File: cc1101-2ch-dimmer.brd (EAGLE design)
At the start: 57.7 x 56.6 mm, 26 parts, among them Q1 IRLZ44, Q2 IRLZ44, U1 ATMEGA328P-AU, U2 0ZCG0035AF2C, U3 173950378, X2 MSTBA2, X3 MSTBA2, X4 MSTBA2

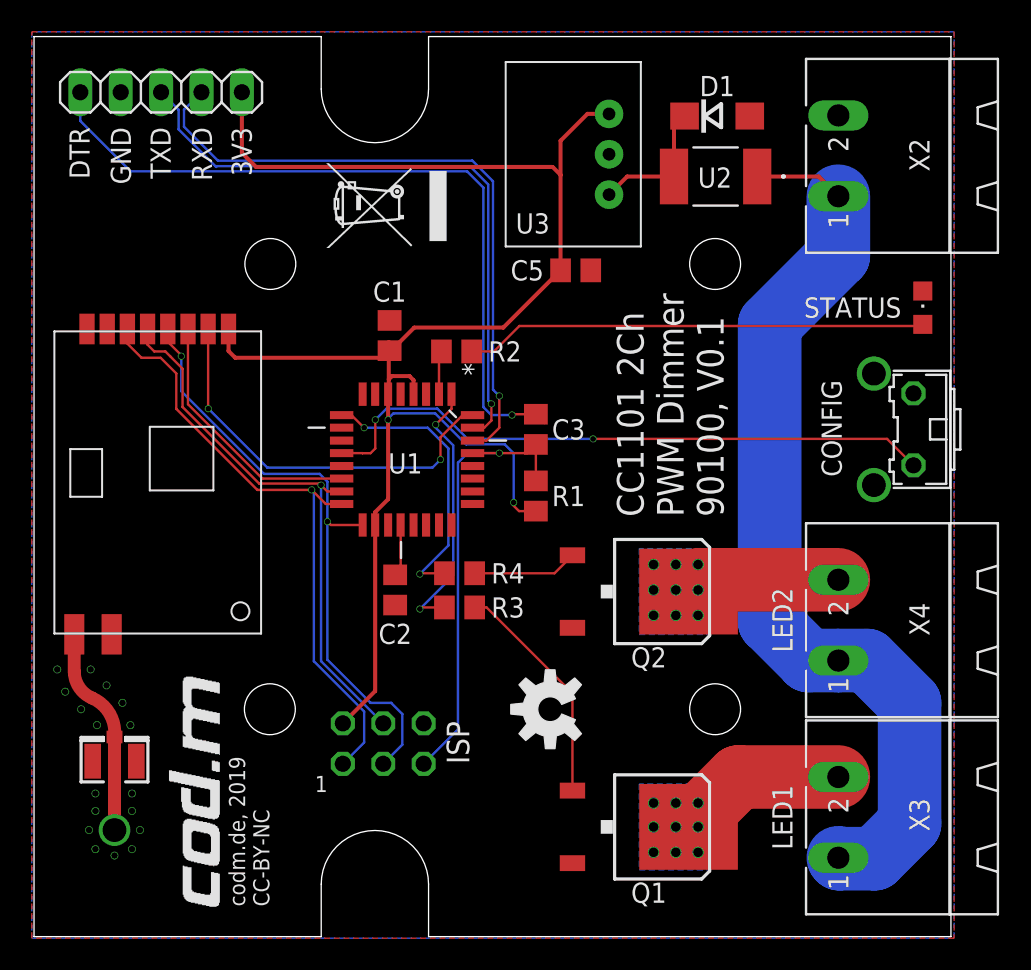
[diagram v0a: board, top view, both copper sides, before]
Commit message: reworked texts
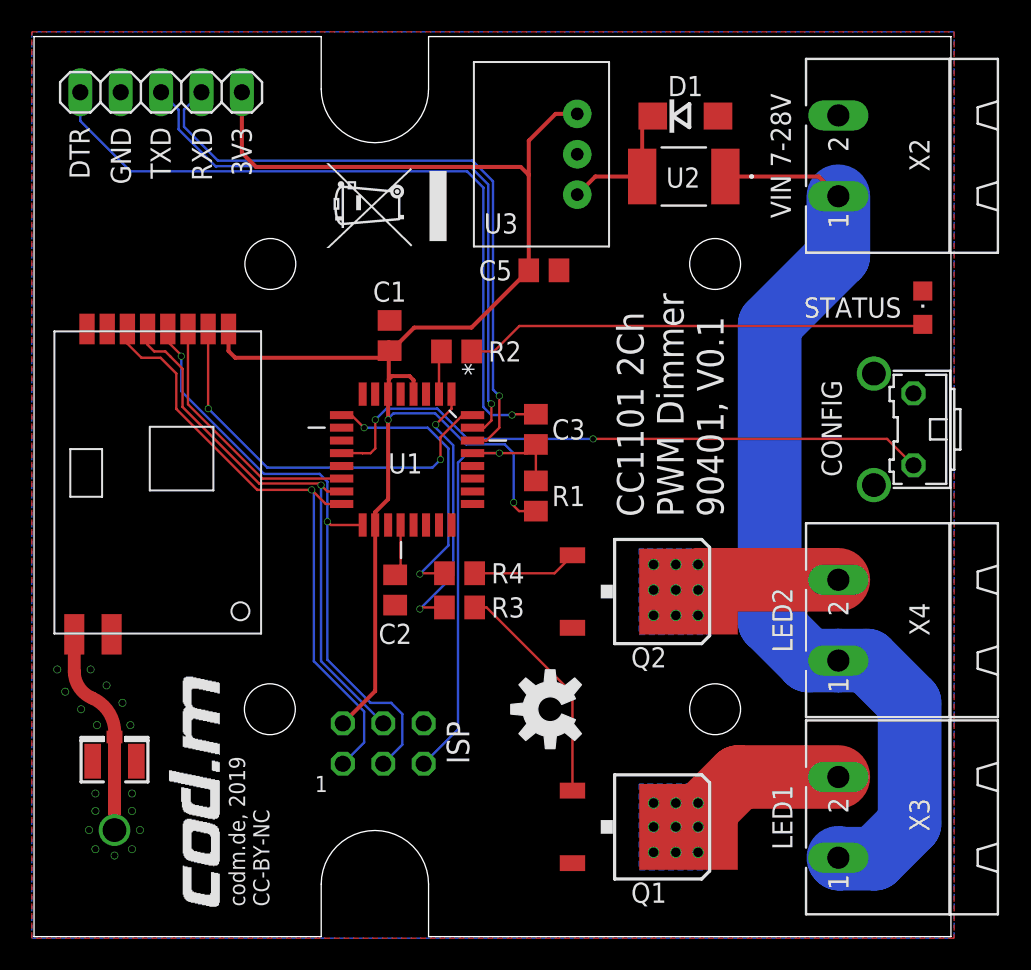
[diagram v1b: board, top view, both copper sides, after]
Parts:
- moved C5 2.00 mm to (32.2, 42.0)
- moved D1 2.00 mm to (41.1, 51.7)
- moved U2 2.00 mm to (41.0, 47.9)
- moved U3 2.00 mm to (36.3, 49.3)
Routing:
- net +3V: track 102.9 -> 98.9 mm
- net VCC: track 58.2 -> 60.2 mm
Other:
- board text added: "CC1101 2Ch PWM Dimmer 90401, V0.1"
- board text added: "VIN 7-28V"
- board text removed: "7-28V"
- board text removed: "CC1101 2Ch PWM Dimmer 90100, V0.1"

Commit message: added 8mhz resonator, reworked for 0.2
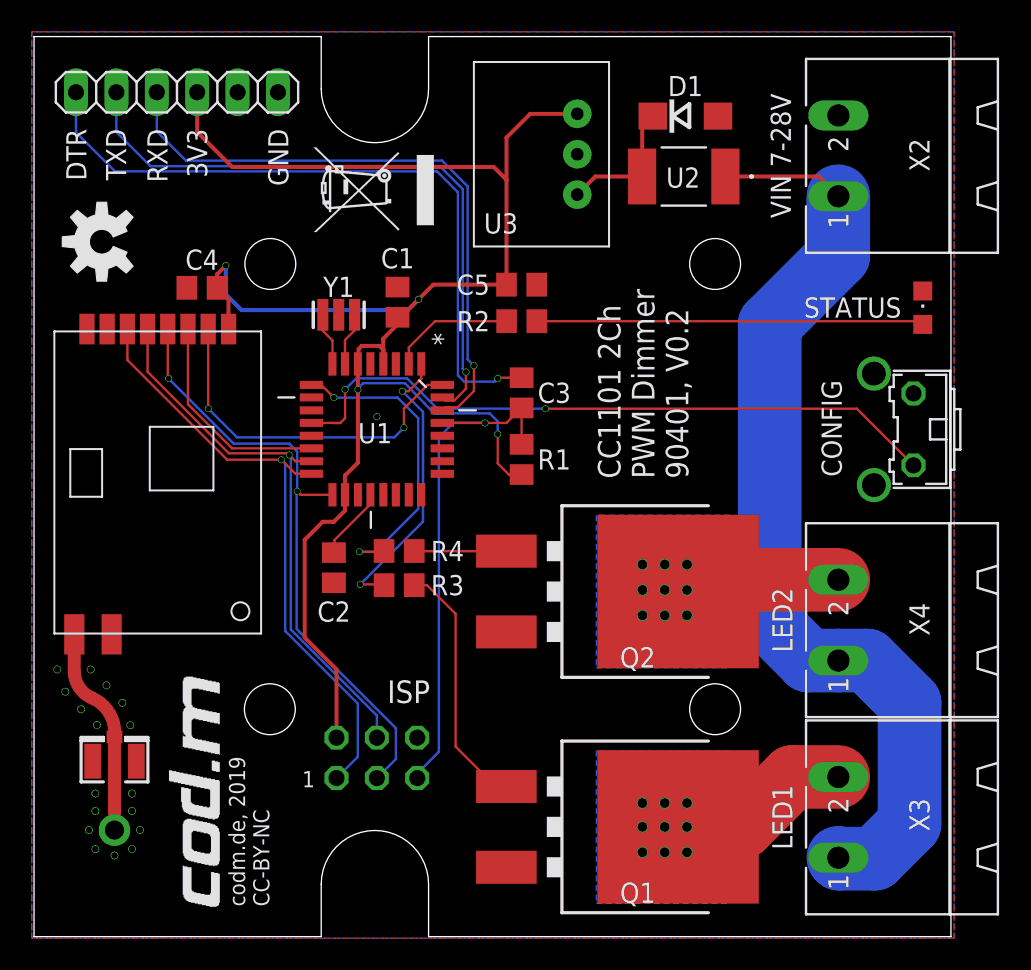
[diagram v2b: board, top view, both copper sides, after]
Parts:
- added C4: 100n, rcl:C0805
- added Y1: CSTCE8M00G52, SmartPrj:RESONATOR
- JP3: device pinhead:1X05 -> pinhead:1X06
- Q1, Q2: value IRLZ44 -> IRLZ44NS; device codm:D-PAK_TO252AA -> codm:D2PAK
- moved LOGO1 40.7 mm to (4.40, 43.8)
- moved R2 4.52 mm to (30.8, 38.8)
- moved C2 4.10 mm to (19.0, 23.3)
- moved R4 4.05 mm to (23.1, 24.4)
- moved R3 4.05 mm to (23.1, 22.2)
- moved U1 2.69 mm to (21.7, 32.0)
- moved R1 2.47 mm to (30.8, 30.1)
- moved C3 2.47 mm to (30.8, 34.3)
- moved C1 2.16 mm to (23.0, 40.0)
- moved C5 1.66 mm to (30.8, 41.1)
- moved U$3 1.28 mm to (25.3, 44.4)
- moved JP3 1.00 mm to (9.13, 53.2)
- moved JP1 0.98 mm to (21.7, 11.3)
- moved Q1 0.70 mm to (38.1, 7.00)
- moved Q2 0.70 mm to (38.1, 21.8)
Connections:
- new net N$4: U1.7, Y1.1
- new net N$7: U1.8, Y1.3
- net +3V: now also C4.2, JP3.3; no longer JP3.1
- net DTR: now also JP3.6; no longer JP3.5
- net GND: now also C4.1, JP3.1, Y1.2; no longer JP3.4
- net LED1: now also Q1.2; no longer Q1.4
- net LED2: now also Q2.2; no longer Q2.4
- net RXD: now also JP3.4; no longer JP3.2
- net TXD: now also JP3.5; no longer JP3.3
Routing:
- net +3V: track 98.9 -> 111.4 mm, vias 2 -> 4
- net N$1: track 2.74 -> 7.87 mm
- net N$2: track 29.1 -> 24.4 mm
- net N$5: track 14.5 -> 19.2 mm
- net RESET: track 29.2 -> 32.9 mm
- net N$4: track 0.00 -> 3.34 mm
- net N$7: track 0.00 -> 3.34 mm
- net DTR: track 47.0 -> 43.9 mm
- net GDO0: track 25.3 -> 22.5 mm
- net CSN: track 16.3 -> 13.6 mm
- net CONFIG: track 39.7 -> 42.3 mm
- net RXD: track 41.2 -> 39.0 mm
- net PWM2: track 17.8 -> 19.7 mm
- net LED1: track 10.7 -> 12.2 mm
- net PWM1: track 16.8 -> 18.3 mm
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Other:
- board text added: "CC1101 2Ch PWM Dimmer 90401, V0.2"
- board text removed: "CC1101 2Ch PWM Dimmer 90401, V0.1"

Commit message: reworked clearance, used newer aisler dru
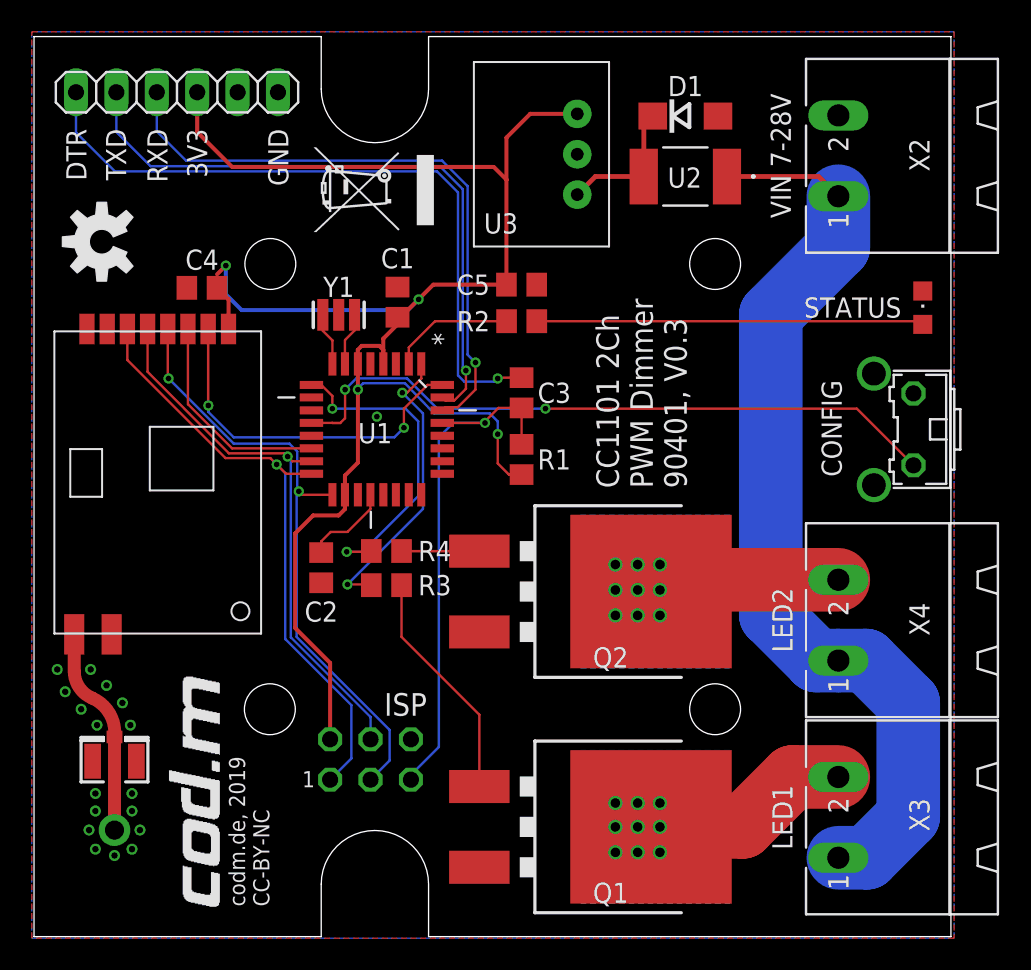
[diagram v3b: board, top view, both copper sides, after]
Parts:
- moved Q1 1.70 mm to (36.4, 7.00)
- moved Q2 1.70 mm to (36.4, 21.8)
- moved C2 0.80 mm to (18.2, 23.3)
- moved R3 0.80 mm to (22.3, 22.2)
- moved R4 0.80 mm to (22.3, 24.4)
- moved JP1 0.41 mm to (21.3, 11.2)
- moved U2 0.10 mm to (41.1, 47.9)
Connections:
- removed net +3V: C1.1, C4.2, C5.2, JP1.2, JP3.3, R1.1, U$1.VCC, U1.18, U1.4, U1.6, U3.P$3
- new net VIN: U2.1, X2.1, X3.1, X4.1
- net VCC: now also C1.1, C4.2, C5.2, JP1.2, JP3.3, R1.1, U$1.VCC, U1.18, U1.4, U1.6, U3.P$3; no longer U2.1, X2.1, X3.1, X4.1
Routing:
- net +3V: track 111.4 -> 0.00 mm, vias 4 -> 0
- net VIN: track 0.00 -> 59.2 mm
- net VCC: track 60.1 -> 111.4 mm, vias 0 -> 4
- net N$5: track 19.2 -> 14.7 mm
- net LED2: track 10.4 -> 12.1 mm
- net LED1: track 12.2 -> 13.9 mm
- net N$6: track 4.57 -> 5.53 mm
- net N$3: track 5.80 -> 4.90 mm
- net PWM2: track 19.7 -> 20.4 mm
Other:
- board text added: "CC1101 2Ch PWM Dimmer 90401, V0.3"
- board text removed: "CC1101 2Ch PWM Dimmer 90401, V0.2"

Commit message: added the chineses cc1101
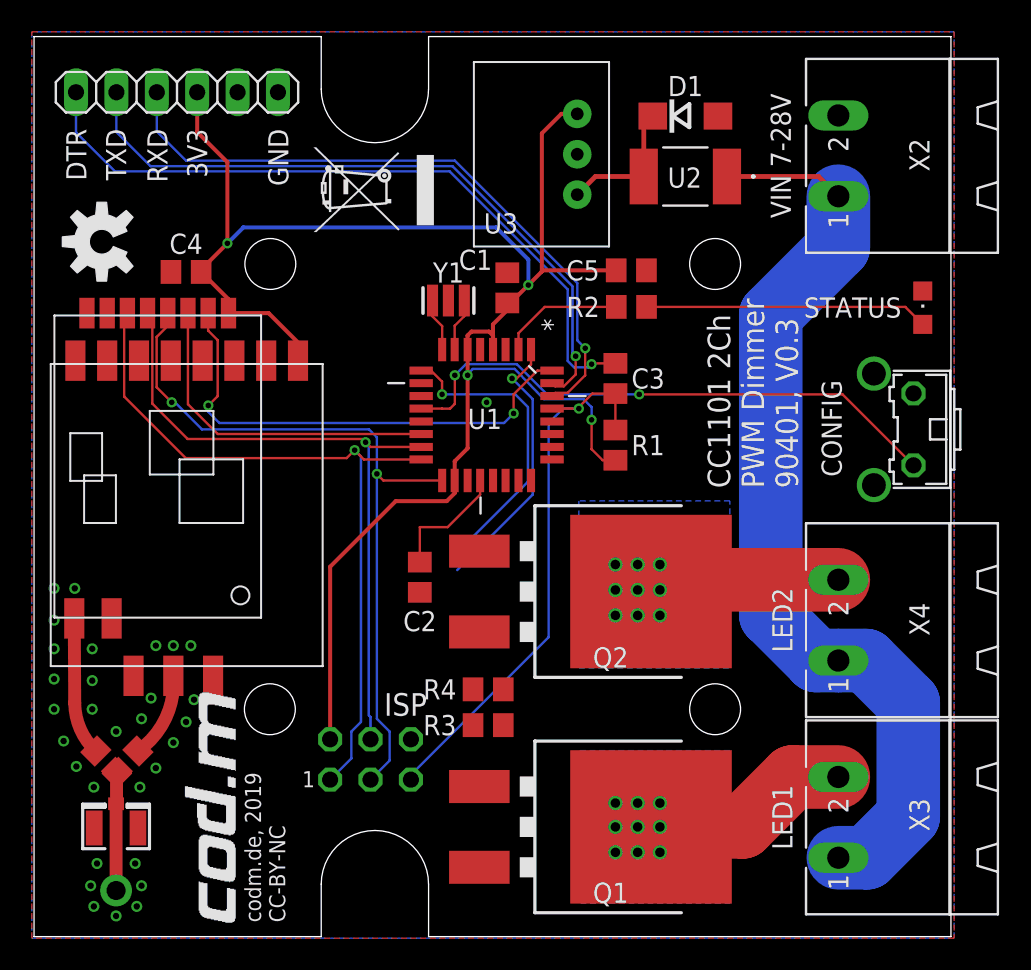
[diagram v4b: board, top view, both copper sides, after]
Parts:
- added R5, R6: 0, rcl:R0805
- added U$4: CC1101-CN-BOARD, codm:CC1101-CN-BOARD
- X1: device adafruit:U.FL -> adafruit-own:U.FL
- moved R3 10.9 mm to (28.7, 13.4), turned to 180 degrees
- moved R4 10.8 mm to (28.7, 15.7), turned to 180 degrees
- moved C5 6.96 mm to (37.7, 42.0)
- moved U1 6.96 mm to (28.6, 32.9)
- moved C1 6.96 mm to (29.9, 40.9)
- moved R2 6.96 mm to (37.7, 39.7)
- moved Y1 6.96 mm to (26.2, 40.1)
- moved C2 6.23 mm to (24.4, 22.7)
- moved C3 5.97 mm to (36.7, 35.2)
- moved R1 5.97 mm to (36.7, 31.0)
- moved X1 4.20 mm to (5.30, 6.93)
- moved C4 1.41 mm to (9.70, 41.9)
- moved U$2 1.41 mm to (12.8, 1.00)
- moved U$1 1.00 mm to (1.42, 39.2)
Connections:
- new net ANT1: R5.1, U$1.ANT
- new net ANT2: R6.2, U$4.ANT
- net ANT: now also R5.2, R6.1; no longer U$1.ANT
- net CSN: now also U$4.CSN
- net GDO0: now also U$4.GDO0
- net GND: now also U$4.GND@1, U$4.GND@2, U$4.GND@3
- net MISO: now also U$4.MISO
- net MOSI: now also U$4.MOSI
- net SCK: now also U$4.SCLK
- net VCC: now also U$4.3V3
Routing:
- net N$5: track 14.7 -> 0.00 mm
- net MISO: track 38.8 -> 47.7 mm
- net ANT1: track 0.00 -> 8.62 mm
- net GDO0: track 22.7 -> 30.7 mm
- net SCK: track 39.0 -> 46.7 mm
- net CSN: track 13.6 -> 21.2 mm
- net MOSI: track 35.3 -> 42.7 mm
- net CONFIG: track 42.3 -> 35.8 mm
- net N$2: track 24.4 -> 17.8 mm
- net ANT: track 13.0 -> 7.44 mm
- net ANT2: track 0.00 -> 5.23 mm
- net N$3: track 4.90 -> 0.00 mm
- net PWM2: track 20.4 -> 17.8 mm, vias 2 -> 1
- net TXD: track 40.3 -> 42.7 mm
- net RXD: track 39.1 -> 41.5 mm
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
